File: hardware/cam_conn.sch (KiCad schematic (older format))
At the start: 1 part, among them J1601 LSHM-150-xxx-x-DV-A-S

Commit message: Fixed Schematic Symbols
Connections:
- wire segments 105 -> 135
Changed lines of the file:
@@
 $Descr A4 11693 8268
 encoding utf-8
-Sheet 16 22
+Sheet 16 21
 Title ""
 Date ""
@@
 Afaik is LVDS Clock optional
 $Comp
-L power1:GND #PWR0218
+L power:GND #PWR0218
 U 1 1 5AFB9A6C
 P 8350 6100
@@
 $EndComp
 $Comp
-L power1:+5V #PWR0219
+L power:+5V #PWR0219
 U 1 1 5AFBA51B
 P 8850 800
@@
 	8350 6100 8350 6050
 Wire Wire Line
-	8850 1550 8850 800
+	8850 1550 8850 1450
 Wire Wire Line
 	8650 2650 8800 2650
 Wire Wire Line
-	8800 2650 8800 6050
-Wire Wire Line
-	8800 6050 7900 6050
+	8800 2650 8800 2950
+Wire Wire Line
+	8800 6050 8350 6050
 Wire Wire Line
 	8650 5650 8800 5650
@@
 	8050 2150 7900 2150
 Wire Wire Line
-	7900 2150 7900 6050
+	7900 2150 7900 2350
 Wire Wire Line
 	8050 5850 7900 5850
@@
 Wire Notes Line
 	10350 1600 10350 2400
+Wire Wire Line
+	8850 1050 8850 950
+Wire Wire Line
+	8850 1150 8850 1050
+Wire Wire Line
+	8850 1250 8850 1150
+Wire Wire Line
+	8850 1350 8850 1250
+Wire Wire Line
+	8850 1450 8850 1350
+Wire Wire Line
+	8850 950  8850 800
+Wire Wire Line
+	8350 6050 7900 6050
+Wire Wire Line
+	8800 5650 8800 6050
+Wire Wire Line
+	8800 5350 8800 5650
+Wire Wire Line
+	8800 5050 8800 5350
+Wire Wire Line
+	8800 4750 8800 5050
+Wire Wire Line
+	8800 4450 8800 4750
+Wire Wire Line
+	8800 4150 8800 4450
+Wire Wire Line
+	8800 3850 8800 4150
+Wire Wire Line
+	8800 3550 8800 3850
+Wire Wire Line
+	8800 3250 8800 3550
+Wire Wire Line
+	8800 2950 8800 3250
+Wire Wire Line
+	7900 5850 7900 6050
+Wire Wire Line
+	7900 5550 7900 5850
+Wire Wire Line
+	7900 5250 7900 5550
+Wire Wire Line
+	7900 4950 7900 5250
+Wire Wire Line
+	7900 4650 7900 4950
+Wire Wire Line
+	7900 4350 7900 4650
+Wire Wire Line
+	7900 4050 7900 4350
+Wire Wire Line
+	7900 3750 7900 4050
+Wire Wire Line
+	7900 3450 7900 3750
+Wire Wire Line
+	7900 3150 7900 3450
+Wire Wire Line
+	7900 2850 7900 3150
+Wire Wire Line
+	7900 2550 7900 2850
+Wire Wire Line
+	7900 2350 7900 2550
 $EndSCHEMATC

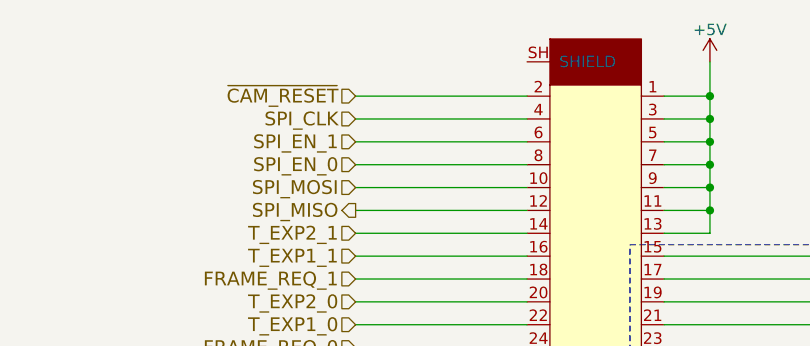
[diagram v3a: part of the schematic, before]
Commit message: WIP: routing the HF Part of the Camera Connector. I have to move the clock away from the left border.
TODO: Fix DDR3 RAM.
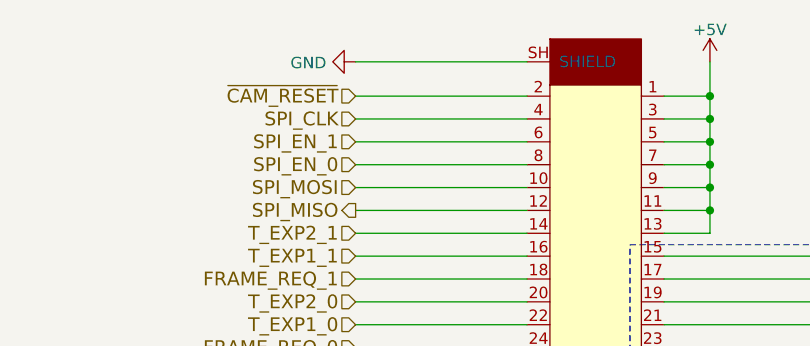
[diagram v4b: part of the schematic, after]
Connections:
- net GND: now also J1601.SH (SHIELD)
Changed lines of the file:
@@
 Wire Wire Line
 	7900 2350 7900 2550
+$Comp
+L power:GND #PWR0198
+U 1 1 5BEC52ED
+P 7300 800
+F 0 "#PWR0198" H 7300 550 50  0001 C CNN
+F 1 "GND" V 7305 672 50  0000 R CNN
+F 2 "" H 7300 800 50  0001 C CNN
+F 3 "" H 7300 800 50  0001 C CNN
+	1    7300 800
+	0    1    1    0
+$EndComp
+Wire Wire Line
+	7300 800  8050 800
 $EndSCHEMATC

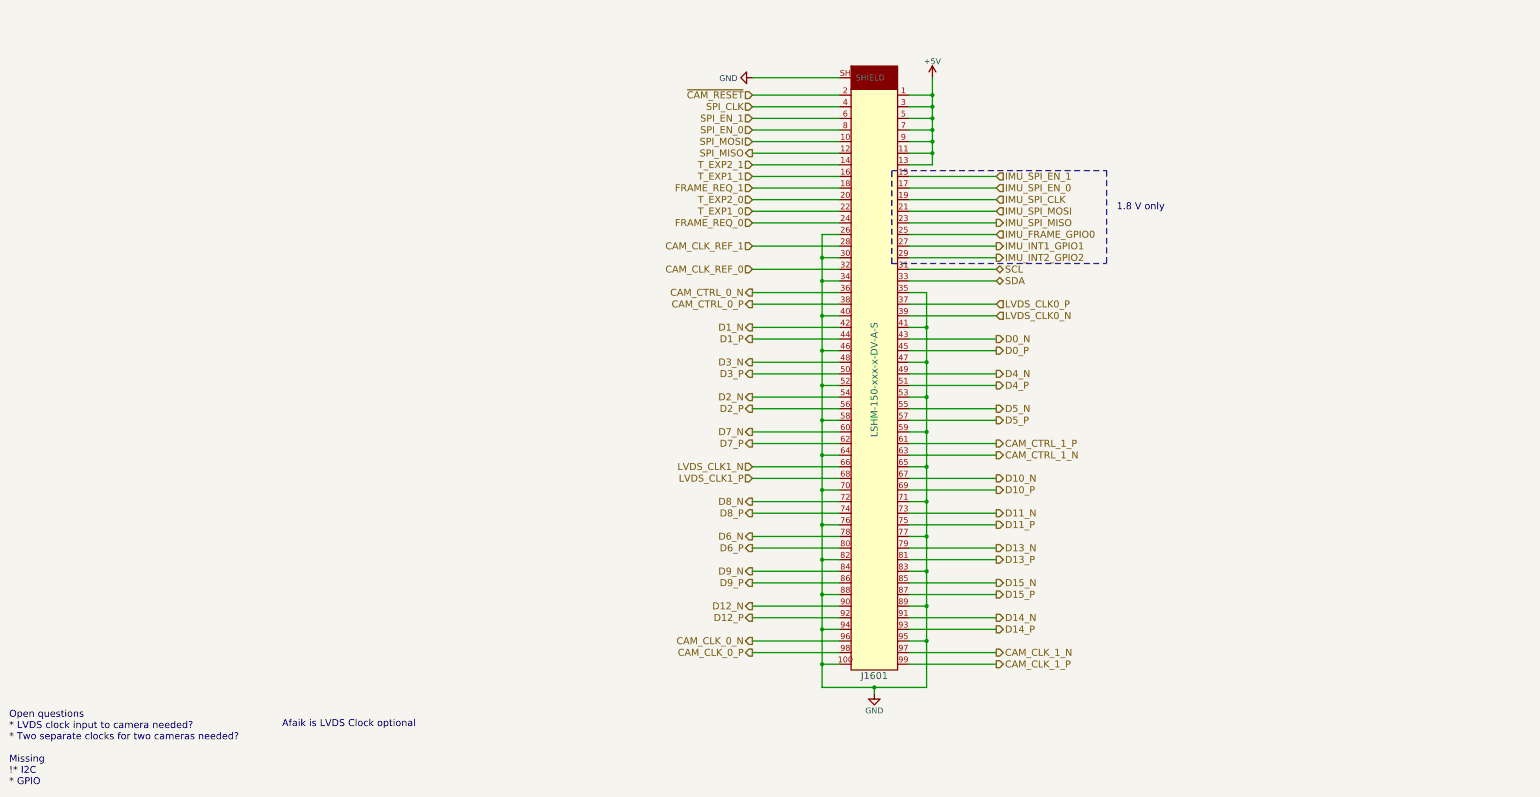
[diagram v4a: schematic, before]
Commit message: Routed a first Version of the High Speed Part of the Camera Connector. The optional LVDS Clocks are left unconnected. I couldn't keep the Connectors Pin Assignment because it was just impossible to route.
WIP: general Routing

Fixed: DDR3 Trace Length Matching
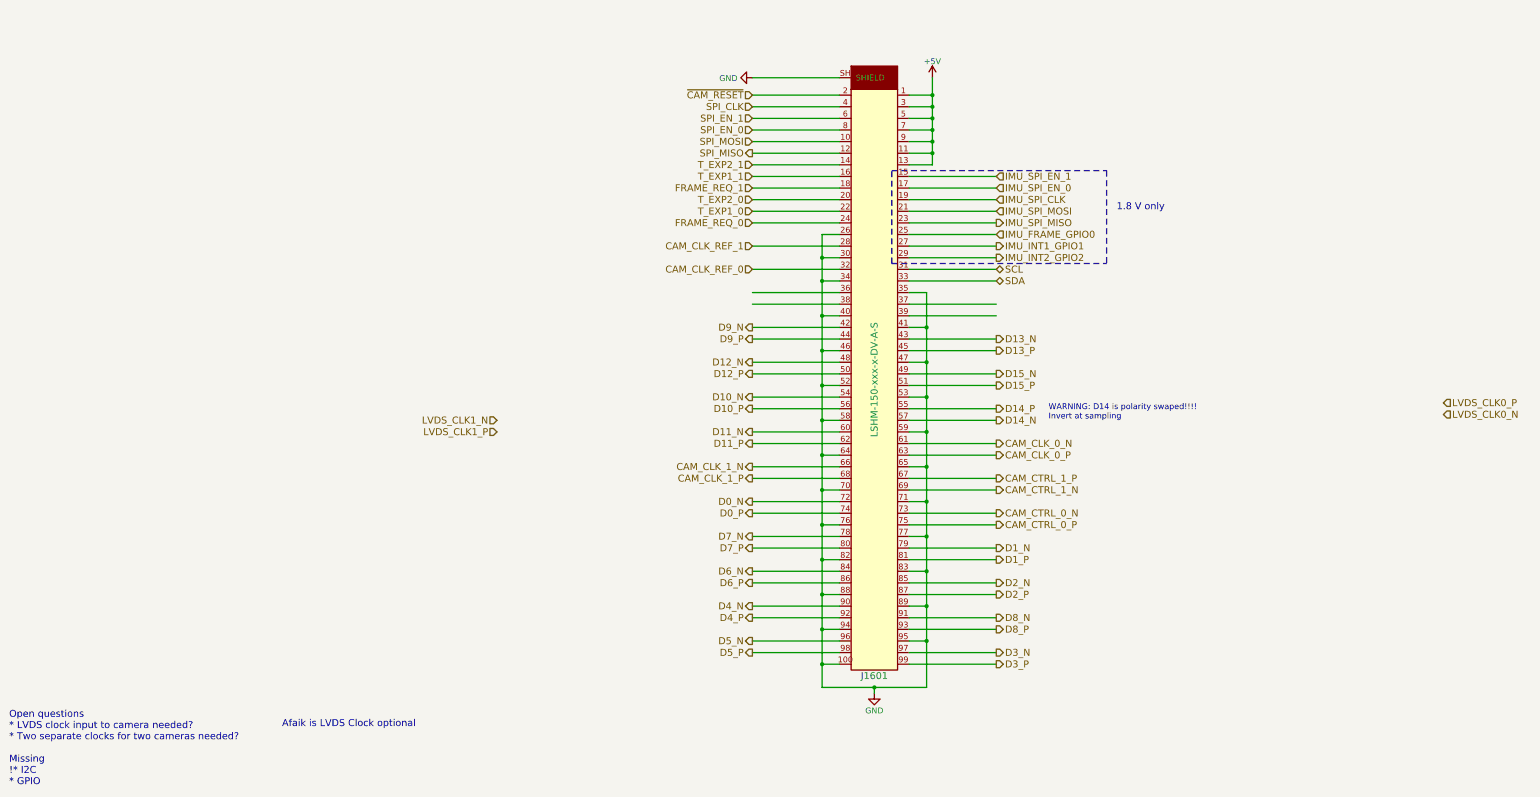
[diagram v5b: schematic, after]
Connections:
- net CAM_CLK_0_N: now also J1601.61; no longer J1601.96
- net CAM_CLK_0_P: now also J1601.63; no longer J1601.98
- net CAM_CLK_1_N: now also J1601.66; no longer J1601.97
- net CAM_CLK_1_P: now also J1601.68; no longer J1601.99
- net CAM_CTRL_0_N: now also J1601.73; no longer J1601.36
- net CAM_CTRL_0_P: now also J1601.75; no longer J1601.38
- net CAM_CTRL_1_N: now also J1601.69; no longer J1601.63
- net CAM_CTRL_1_P: now also J1601.67; no longer J1601.61
- net D0_N: now also J1601.72; no longer J1601.43
- net D0_P: now also J1601.74; no longer J1601.45
- net D10_N: now also J1601.54; no longer J1601.67
- net D10_P: now also J1601.56; no longer J1601.69
- net D11_N: now also J1601.60; no longer J1601.73
- net D11_P: now also J1601.62; no longer J1601.75
- net D12_N: now also J1601.48; no longer J1601.90
- net D12_P: now also J1601.50; no longer J1601.92
- net D13_N: now also J1601.43; no longer J1601.79
- net D13_P: now also J1601.45; no longer J1601.81
- net D14_N: now also J1601.57; no longer J1601.91
- net D14_P: now also J1601.55; no longer J1601.93
- net D15_N: now also J1601.49; no longer J1601.85
- net D15_P: now also J1601.51; no longer J1601.87
- net D1_N: now also J1601.79; no longer J1601.42
- net D1_P: now also J1601.81; no longer J1601.44
- net D2_N: now also J1601.85; no longer J1601.54
- net D2_P: now also J1601.87; no longer J1601.56
- net D3_N: now also J1601.97; no longer J1601.48
- net D3_P: now also J1601.99; no longer J1601.50
- net D4_N: now also J1601.90; no longer J1601.49
- net D4_P: now also J1601.92; no longer J1601.51
- net D5_N: now also J1601.96; no longer J1601.55
- net D5_P: now also J1601.98; no longer J1601.57
- net D6_N: now also J1601.84; no longer J1601.78
- net D6_P: now also J1601.86; no longer J1601.80
- net D7_N: now also J1601.78; no longer J1601.60
- net D7_P: now also J1601.80; no longer J1601.62
- net D8_N: now also J1601.91; no longer J1601.72
- net D8_P: now also J1601.93; no longer J1601.74
- net D9_N: now also J1601.42; no longer J1601.84
- net D9_P: now also J1601.44; no longer J1601.86
- net LVDS_CLK0_N: no longer J1601.39
- net LVDS_CLK0_P: no longer J1601.37
- net LVDS_CLK1_N: no longer J1601.66
- net LVDS_CLK1_P: no longer J1601.68
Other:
- note added: "WARNING: D14 is polarity swaped!!!!\nInvert at sampling"
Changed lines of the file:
@@
 $Descr A4 11693 8268
 encoding utf-8
-Sheet 15 21
+Sheet 14 21
 Title ""
 Date ""
@@
 Comment4 ""
 $EndDescr
-Text HLabel 9400 5750 2    60   Output ~ 0
+Text HLabel 7300 4150 0    60   Output ~ 0
 CAM_CLK_1_N
-Text HLabel 7300 5750 0    60   Output ~ 0
+Text HLabel 9400 4050 2    60   Output ~ 0
 CAM_CLK_0_P
-Text HLabel 7300 5650 0    60   Output ~ 0
+Text HLabel 9400 3950 2    60   Output ~ 0
 CAM_CLK_0_N
-Text HLabel 9400 5850 2    60   Output ~ 0
+Text HLabel 7300 4250 0    60   Output ~ 0
 CAM_CLK_1_P
 Text HLabel 7300 2050 0    60   Input ~ 0
@@
 Text HLabel 7300 1550 0    60   Input ~ 0
 T_EXP2_1
-Text HLabel 7300 2750 0    60   Output ~ 0
+Text HLabel 9400 4650 2    60   Output ~ 0
 CAM_CTRL_0_P
-Text HLabel 7300 2650 0    60   Output ~ 0
+Text HLabel 9400 4550 2    60   Output ~ 0
 CAM_CTRL_0_N
-Text HLabel 9400 3950 2    60   Output ~ 0
+Text HLabel 9400 4250 2    60   Output ~ 0
 CAM_CTRL_1_P
-Text HLabel 9400 4050 2    60   Output ~ 0
+Text HLabel 9400 4350 2    60   Output ~ 0
 CAM_CTRL_1_N
 Text HLabel 7300 1450 0    60   Output ~ 0
@@
 	1    0    0    -1
 $EndComp
+Text HLabel 7300 4450 0    60   Output ~ 0
+D0_N
+Text HLabel 7300 4550 0    60   Output ~ 0
+D0_P
+Text HLabel 9400 4850 2    60   Output ~ 0
+D1_N
+Text HLabel 9400 4950 2    60   Output ~ 0
+D1_P
+Text HLabel 9400 5150 2    60   Output ~ 0
+D2_N
+Text HLabel 9400 5250 2    60   Output ~ 0
+D2_P
+Text HLabel 9400 5750 2    60   Output ~ 0
+D3_N
+Text HLabel 9400 5850 2    60   Output ~ 0
+D3_P
+Text HLabel 7300 5350 0    60   Output ~ 0
+D4_N
+Text HLabel 7300 5450 0    60   Output ~ 0
+D4_P
+Text HLabel 7300 5650 0    60   Output ~ 0
+D5_N
+Text HLabel 7300 5750 0    60   Output ~ 0
+D5_P
+Text HLabel 7300 5050 0    60   Output ~ 0
+D6_N
+Text HLabel 7300 5150 0    60   Output ~ 0
+D6_P
+Text HLabel 7300 4750 0    60   Output ~ 0
+D7_N
+Text HLabel 7300 4850 0    60   Output ~ 0
+D7_P
+Text HLabel 9400 5450 2    60   Output ~ 0
+D8_N
+Text HLabel 9400 5550 2    60   Output ~ 0
+D8_P
+Text HLabel 7300 2950 0    60   Output ~ 0
+D9_N
+Text HLabel 7300 3050 0    60   Output ~ 0
+D9_P
+Text HLabel 7300 3550 0    60   Output ~ 0
+D10_N
+Text HLabel 7300 3650 0    60   Output ~ 0
+D10_P
+Text HLabel 7300 3850 0    60   Output ~ 0
+D11_N
+Text HLabel 7300 3950 0    60   Output ~ 0
+D11_P
+Text HLabel 7300 3250 0    60   Output ~ 0
+D12_N
+Text HLabel 7300 3350 0    60   Output ~ 0
+D12_P
 Text HLabel 9400 3050 2    60   Output ~ 0
-D0_N
+D13_N
 Text HLabel 9400 3150 2    60   Output ~ 0
-D0_P
-Text HLabel 7300 2950 0    60   Output ~ 0
-D1_N
-Text HLabel 7300 3050 0    60   Output ~ 0
-D1_P
-Text HLabel 7300 3550 0    60   Output ~ 0
-D2_N
-Text HLabel 7300 3650 0    60   Output ~ 0
-D2_P
-Text HLabel 7300 3250 0    60   Output ~ 0
-D3_N
-Text HLabel 7300 3350 0    60   Output ~ 0
-D3_P
+D13_P
+Text HLabel 9400 3750 2    60   Output ~ 0
+D14_N
+Text HLabel 9400 3650 2    60   Output ~ 0
+D14_P
 Text HLabel 9400 3350 2    60   Output ~ 0
-D4_N
+D15_N
 Text HLabel 9400 3450 2    60   Output ~ 0
-D4_P
-Text HLabel 9400 3650 2    60   Output ~ 0
-D5_N
-Text HLabel 9400 3750 2    60   Output ~ 0
-D5_P
-Text HLabel 7300 4750 0    60   Output ~ 0
-D6_N
-Text HLabel 7300 4850 0    60   Output ~ 0
-D6_P
-Text HLabel 7300 3850 0    60   Output ~ 0
-D7_N
-Text HLabel 7300 3950 0    60   Output ~ 0
-D7_P
-Text HLabel 7300 4450 0    60   Output ~ 0
-D8_N
-Text HLabel 7300 4550 0    60   Output ~ 0
-D8_P
-Text HLabel 7300 5050 0    60   Output ~ 0
-D9_N
-Text HLabel 7300 5150 0    60   Output ~ 0
-D9_P
-Text HLabel 9400 4250 2    60   Output ~ 0
-D10_N
-Text HLabel 9400 4350 2    60   Output ~ 0
-D10_P
-Text HLabel 9400 4550 2    60   Output ~ 0
-D11_N
-Text HLabel 9400 4650 2    60   Output ~ 0
-D11_P
-Text HLabel 7300 5350 0    60   Output ~ 0
-D12_N
-Text HLabel 7300 5450 0    60   Output ~ 0
-D12_P
-Text HLabel 9400 4850 2    60   Output ~ 0
-D13_N
-Text HLabel 9400 4950 2    60   Output ~ 0
-D13_P
-Text HLabel 9400 5450 2    60   Output ~ 0
-D14_N
-Text HLabel 9400 5550 2    60   Output ~ 0
-D14_P
-Text HLabel 9400 5150 2    60   Output ~ 0
-D15_N
-Text HLabel 9400 5250 2    60   Output ~ 0
 D15_P
 Text HLabel 9400 2050 2    60   Output ~ 0
@@
 Text HLabel 9400 2350 2    60   Output ~ 0
 IMU_INT2_GPIO2
-Text HLabel 9400 2850 2    60   Input ~ 0
+Text HLabel 13250 3700 2    60   Input ~ 0
 LVDS_CLK0_N
-Text HLabel 9400 2750 2    60   Input ~ 0
+Text HLabel 13250 3600 2    60   Input ~ 0
 LVDS_CLK0_P
-Text HLabel 7300 4150 0    60   Input ~ 0
+Text HLabel 5100 3750 0    60   Input ~ 0
 LVDS_CLK1_N
-Text HLabel 7300 4250 0    60   Input ~ 0
+Text HLabel 5100 3850 0    60   Input ~ 0
 LVDS_CLK1_P
 Wire Wire Line
@@
 Wire Wire Line
 	7300 800  8050 800
+Text Notes 9850 3750 0    50   ~ 0
+WARNING: D14 is polarity swaped!!!!\nInvert at sampling
 $EndSCHEMATC

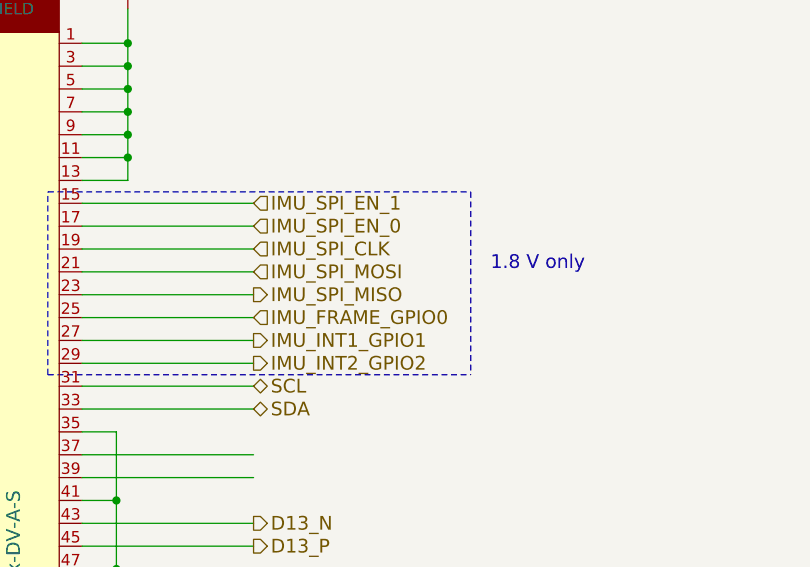
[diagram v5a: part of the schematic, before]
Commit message: Added Courtyard to selfmade Footprints. Also general Routing WIP.
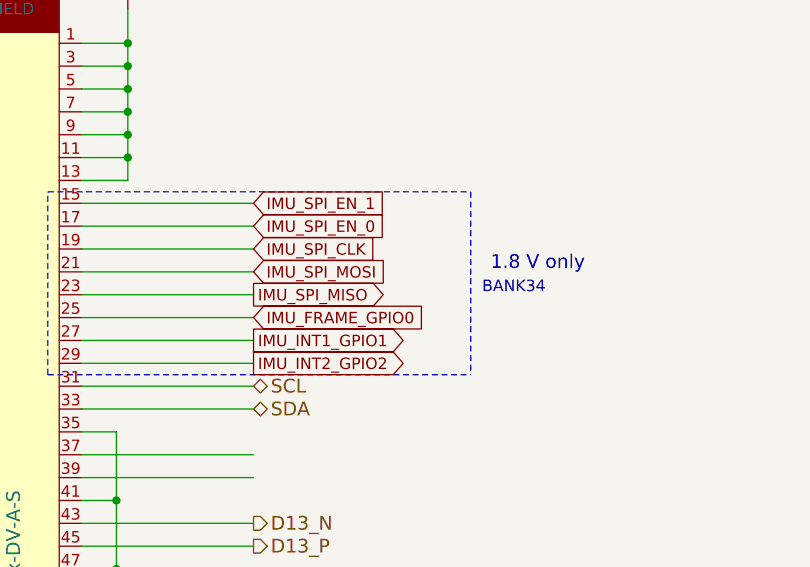
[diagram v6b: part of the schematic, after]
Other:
- note added: "BANK34"
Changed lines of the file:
@@
 EESchema Schematic File Version 4
+LIBS:zynq_board-cache
 EELAYER 26 0
 EELAYER END
@@
 Text HLabel 9400 3450 2    60   Output ~ 0
 D15_P
-Text HLabel 9400 2050 2    60   Output ~ 0
-IMU_SPI_MISO
-Text HLabel 9400 1950 2    60   Input ~ 0
-IMU_SPI_MOSI
-Text HLabel 9400 1850 2    60   Input ~ 0
-IMU_SPI_CLK
-Text HLabel 9400 1750 2    60   Input ~ 0
-IMU_SPI_EN_0
-Text HLabel 9400 1650 2    60   Input ~ 0
-IMU_SPI_EN_1
 Text Notes 10850 1950 2    60   ~ 0
 1.8 V only
 Text HLabel 7300 2250 0    60   Input ~ 0
 CAM_CLK_REF_1
-Text HLabel 9400 2150 2    60   Input ~ 0
-IMU_FRAME_GPIO0
-Text HLabel 9400 2250 2    60   Output ~ 0
-IMU_INT1_GPIO1
-Text HLabel 9400 2350 2    60   Output ~ 0
-IMU_INT2_GPIO2
 Text HLabel 13250 3700 2    60   Input ~ 0
 LVDS_CLK0_N
@@
 Text Notes 9850 3750 0    50   ~ 0
 WARNING: D14 is polarity swaped!!!!\nInvert at sampling
+Text GLabel 9400 1650 2    50   Input ~ 0
+IMU_SPI_EN_1
+Text GLabel 9400 1750 2    50   Input ~ 0
+IMU_SPI_EN_0
+Text GLabel 9400 1850 2    50   Input ~ 0
+IMU_SPI_CLK
+Text GLabel 9400 1950 2    50   Input ~ 0
+IMU_SPI_MOSI
+Text GLabel 9400 2050 2    50   Output ~ 0
+IMU_SPI_MISO
+Text GLabel 9400 2150 2    50   Input ~ 0
+IMU_FRAME_GPIO0
+Text GLabel 9400 2250 2    50   Output ~ 0
+IMU_INT1_GPIO1
+Text GLabel 9400 2350 2    50   Output ~ 0
+IMU_INT2_GPIO2
+Text Notes 10400 2050 0    50   ~ 0
+BANK34
 $EndSCHEMATC

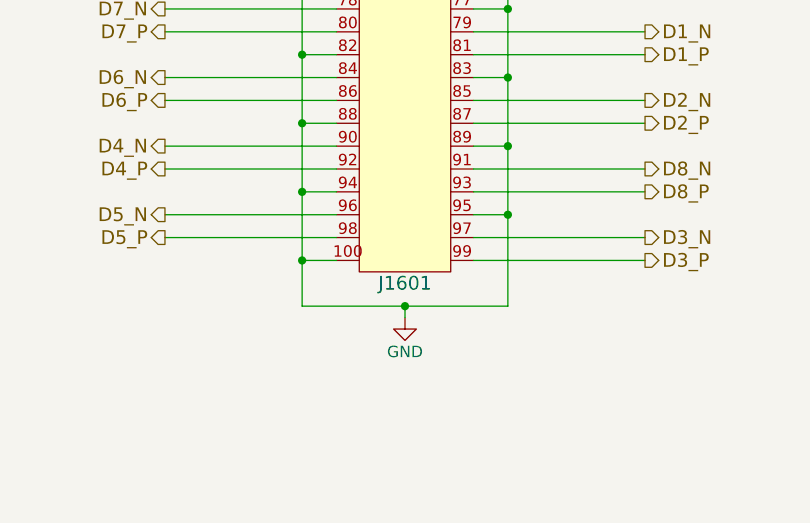
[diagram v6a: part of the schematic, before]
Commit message: Routed extra GPIO Solder Pads, reannotated the whole schematic to make it consistent.
Power Distribution routing WIP
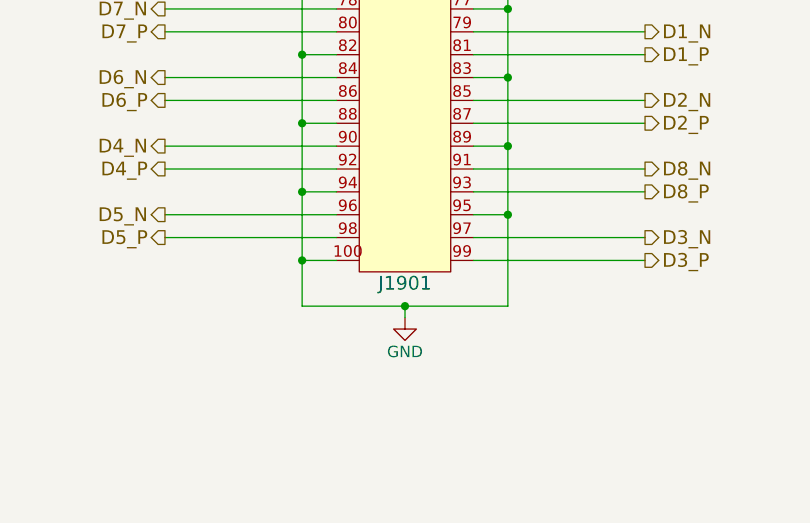
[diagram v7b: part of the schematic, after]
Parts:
- renumbered J1601 to J1901
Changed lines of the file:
@@
 $Descr A4 11693 8268
 encoding utf-8
-Sheet 14 21
+Sheet 19 21
 Title ""
 Date ""
@@
 Open questions\n* LVDS clock input to camera needed?\n* Two separate clocks for two cameras needed?\n\nMissing\n!* I2C\n* GPIO
 $Comp
-L lshm-150-xxx-x-dv-a-s:LSHM-150-xxx-x-DV-A-S J1601
+L lshm-150-xxx-x-dv-a-s:LSHM-150-xxx-x-DV-A-S J1901
 U 1 1 5ACC34F1
 P 8350 3400
-F 0 "J1601" H 8350 850 60  0000 C CNN
+F 0 "J1901" H 8350 850 60  0000 C CNN
 F 1 "LSHM-150-xxx-x-DV-A-S" V 8350 3400 60  0000 C CNN
 F 2 "Connectors_Samtec:LSHM-150-xxx-x-DV-A-S" H 8350 4550 60  0001 C CNN
@@
 Afaik is LVDS Clock optional
 $Comp
-L power:GND #PWR0218
+L power:GND #PWR01902
 U 1 1 5AFB9A6C
 P 8350 6100
-F 0 "#PWR0218" H 8350 5850 50  0001 C CNN
+F 0 "#PWR01902" H 8350 5850 50  0001 C CNN
 F 1 "GND" H 8350 5950 50  0000 C CNN
 F 2 "" H 8350 6100 50  0001 C CNN
@@
 $EndComp
 $Comp
-L power:+5V #PWR0219
+L power:+5V #PWR01903
 U 1 1 5AFBA51B
 P 8850 800
-F 0 "#PWR0219" H 8850 650 50  0001 C CNN
+F 0 "#PWR01903" H 8850 650 50  0001 C CNN
 F 1 "+5V" H 8850 940 50  0000 C CNN
 F 2 "" H 8850 800 50  0001 C CNN
@@
 	7900 2350 7900 2550
 $Comp
-L power:GND #PWR0198
+L power:GND #PWR01901
 U 1 1 5BEC52ED
 P 7300 800
-F 0 "#PWR0198" H 7300 550 50  0001 C CNN
+F 0 "#PWR01901" H 7300 550 50  0001 C CNN
 F 1 "GND" V 7305 672 50  0000 R CNN
 F 2 "" H 7300 800 50  0001 C CNN
